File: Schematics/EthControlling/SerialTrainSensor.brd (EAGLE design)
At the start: 13 x 23 mm, 18 parts, among them IC1 ATTINY10, IC2 LMV358, IC3 ATTINY10

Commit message: restore repository
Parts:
- removed IC1, IC3: ATTINY10, myparts:SOT-23
- removed JP1, JP2: SERIAL_SENSOR, myparts:SERIAL_4
- added SMD1, SMD2: SERIAL_SENSORTH, myparts:SERIAL_5_THROUGH
- added U$1, U$2: ATTINY10, myparts:SOT-23
- moved C1 4.81 mm to (8.59, 12.3), turned to 0 degrees
- moved C3 4.57 mm to (8.45, 10.2), turned to 180 degrees
- moved R2 3.71 mm to (2.03, 20.7), turned to 90 degrees
- moved IC2 0.73 mm to (4.27, 12.0)
- moved R1 0.45 mm to (4.37, 18.1)
- moved R3 0.29 mm to (4.37, 16.5)
- moved C2 0.20 mm to (6.30, 11.3)
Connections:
- net CHAIN_IN: now also SMD2.P$4, U$1.3; no longer IC1.3, JP2.4
- net CHAIN_OUT: now also SMD1.P$4, U$2.4; no longer IC3.4, JP1.4
- net GND: now also R5.1, SMD1.P$5, SMD2.P$5, U$1.2, U$2.2; no longer IC1.5, IC3.5, JP1.5, JP2.5, R3.1, R4.1, R5.2, U$100.2, U$101.2
- net N$4: now also U$1.4, U$2.3; no longer IC1.4, IC3.3
- net SENS_A: now also R3.1, U$1.1; no longer IC1.1
- net SENS_B: now also R4.1, R5.2, U$2.1; no longer IC3.1, R5.1
- net TRANS: now also SMD1.P$3, SMD2.P$3, U$1.6, U$2.6; no longer IC1.6, IC3.6, JP1.3, JP2.3
- net VCC: now also D1.A, D2.A, SMD1.P$2, SMD2.P$2, U$1.5, U$2.5; no longer IC1.2, IC3.2, JP1.2, JP2.2
- net VLED: now also SMD1.P$1, SMD2.P$1, U$100.2, U$101.2; no longer D1.A, D2.A, JP1.1, JP2.1
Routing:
- net VCC: track 48.6 -> 0.00 mm, vias 5 -> 0
- net VLED: track 32.0 -> 0.00 mm, vias 3 -> 0
- net GND: track 25.0 -> 0.00 mm, vias 8 -> 0
- net CHAIN_IN: track 19.6 -> 0.00 mm, vias 2 -> 0
- net CHAIN_OUT: track 17.8 -> 0.00 mm, vias 2 -> 0
- net TRANS: track 17.4 -> 0.00 mm, vias 2 -> 0
- net SENS_A: track 15.0 -> 0.00 mm, vias 2 -> 0
- net N$2: track 13.8 -> 0.00 mm, vias 2 -> 0
- net N$5: track 12.3 -> 0.00 mm
- net SENS_B: track 11.6 -> 0.00 mm
- net N$4: track 11.4 -> 0.00 mm, vias 2 -> 0
- net N$1: track 4.23 -> 0.00 mm
- net N$3: track 3.61 -> 0.00 mm
- net N$6: track 2.31 -> 0.00 mm
- net N$7: track 1.80 -> 0.00 mm
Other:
- board text added: "TrainSerialSensor Rev.B"
- board text removed: "D45497"
- board text removed: "TrainSerialSensor Rev.A"

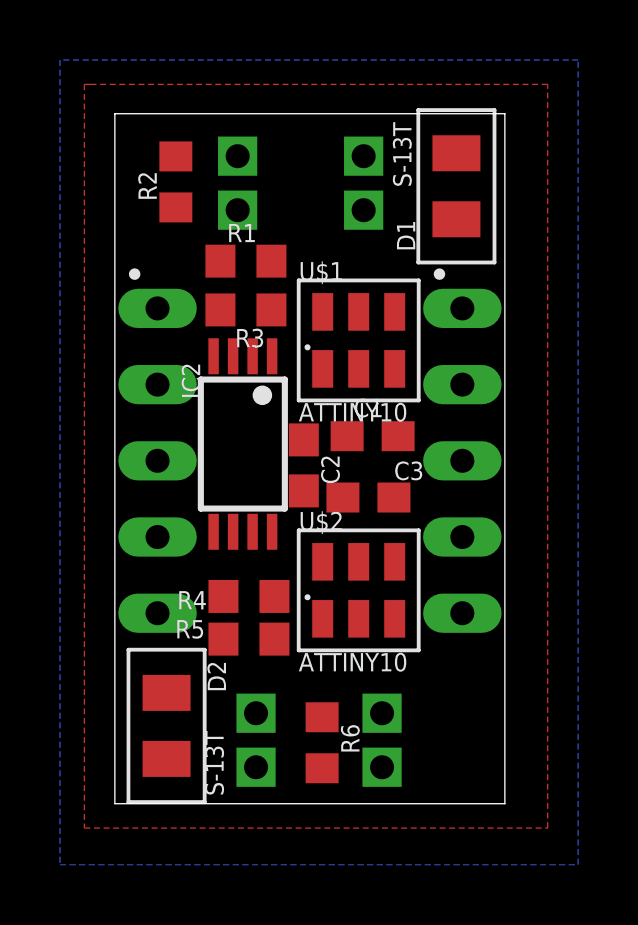
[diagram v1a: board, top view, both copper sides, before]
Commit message: wired SerialTrainSensor RevB
Signed-off-by: sosoru <siva6991@yahoo.co.jp>
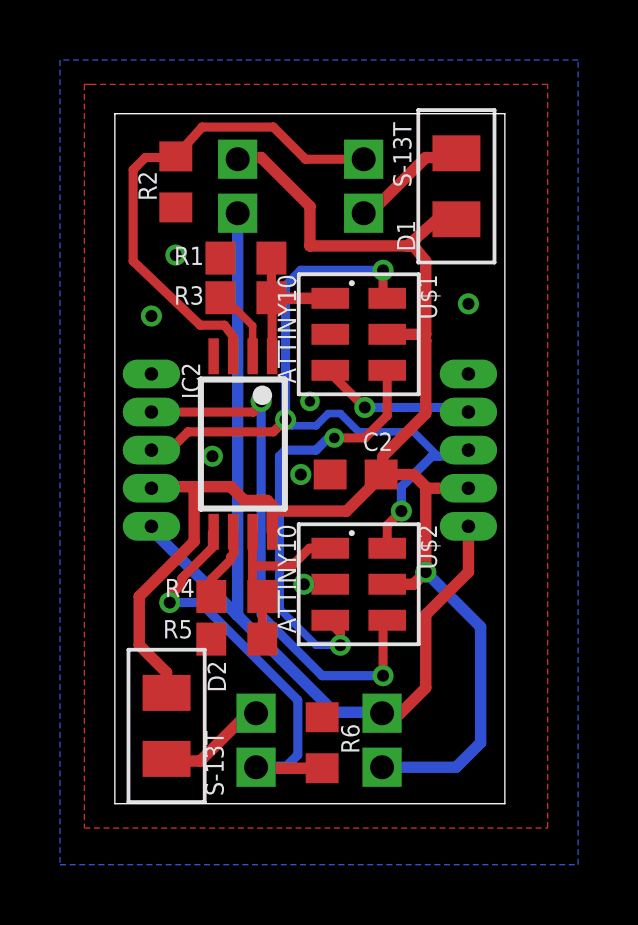
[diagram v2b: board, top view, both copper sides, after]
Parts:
- removed C1, C3: 0.1u, rcl:C0603
- SMD1, SMD2: value SERIAL_SENSORTH -> SERIAL_SENSORHALF; device myparts:SERIAL_5_THROUGH -> myparts:SERIAL_5_HALF
- moved C2 1.75 mm to (8.03, 11.0), turned to 180 degrees
- moved SMD1 1.64 mm to (11.8, 11.8), turned to 90 degrees
- moved SMD2 1.64 mm to (1.22, 11.8), turned to 90 degrees
- moved R3 0.41 mm to (4.37, 16.9)
- moved R4 0.41 mm to (4.06, 6.91)
- moved R5 0.41 mm to (4.06, 5.49)
- moved U$1 0.20 mm to (8.13, 15.6), turned to 270 degrees
- moved U$2 0.20 mm to (8.13, 7.32), turned to 270 degrees
- moved U$101 0.10 mm to (5.59, 21.2)
- moved R1 0.10 mm to (4.37, 18.2), turned to 180 degrees
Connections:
- net CHAIN_IN: now also SMD1.P$4; no longer SMD2.P$4
- net CHAIN_OUT: now also SMD2.P$4; no longer SMD1.P$4
- net GND: no longer C1.2, C3.2
- net VCC: no longer C1.1, C3.1
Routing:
- net VCC: track 0.00 -> 55.0 mm, vias 0 -> 1
- net VLED: track 0.00 -> 31.6 mm
- net TRANS: track 0.00 -> 24.9 mm, vias 0 -> 3
- net CHAIN_OUT: track 0.00 -> 17.8 mm, vias 0 -> 2
- net N$2: track 0.00 -> 16.8 mm
- net N$4: track 0.00 -> 14.4 mm, vias 0 -> 2
- net N$5: track 0.00 -> 14.2 mm, vias 0 -> 1
- net SENS_B: track 0.00 -> 6.54 mm
- net SENS_A: track 0.00 -> 6.00 mm
- net CHAIN_IN: track 0.00 -> 5.27 mm, vias 0 -> 1
- net N$1: track 0.00 -> 3.89 mm
- net N$3: track 0.00 -> 3.67 mm
- net N$6: track 0.00 -> 2.48 mm
- net N$7: track 0.00 -> 2.47 mm
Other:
- board text added: "TrSensor Rev.B"
- board text removed: "TrainSerialSensor Rev.B"

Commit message: ditto
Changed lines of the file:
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@@
 <wire x1="8.89" y1="3.048" x2="8.9064" y2="3.0156" width="0.381" layer="16"/>
 <wire x1="4.0936" y1="6.3288" x2="4.064" y2="6.2992" width="0.381" layer="16"/>
-<wire x1="1.2192" y1="9.144" x2="1.2192" y2="9.2456" width="0" layer="19" extent="16-16"/>
+<wire x1="1.2192" y1="9.2456" x2="1.2192" y2="9.144" width="0.381" layer="16"/>
 </signal>
 <signal name="N$4">

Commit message: ditto
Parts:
- added R7: (no value), rcl:R0603
- moved C2 0.64 mm to (8.64, 10.8)
- moved U$1 0.62 mm to (8.23, 16.3)
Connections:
- net N$4: now also R7.2
- net VCC: now also R7.1
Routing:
- net GND: track 0.00 -> 1.04 mm
- net TRANS: track 24.9 -> 24.2 mm
- net N$4: track 14.4 -> 15.0 mm
- net CHAIN_IN: track 5.27 -> 5.78 mm
